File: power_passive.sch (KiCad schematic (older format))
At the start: 39 parts, among them J10 Conn_01x02, J11 Conn_01x02, J12 Conn_01x02, J13 Conn_01x02, J14 Conn_01x02, J15 Conn_01x02, J16 Conn_01x02, J17 Conn_01x02, J18 Conn_01x02, J19 Conn_01x02, J20 Conn_01x02, J5 ATX-24, J6 Conn_01x02, J7 Conn_01x02, J8 Conn_01x02, J9 Conn_01x02, Q1 MMBT4401-7-F, Q10 MMBT4401-7-F, Q11 SI7113ADN-T1-GE3, Q2 MMBT4401-7-F, Q3 MMBT4401-7-F, Q4 SI7113ADN-T1-GE3, Q5 SI7113ADN-T1-GE3, Q6 MMBT4401-7-F, Q7 MMBT4401-7-F, Q8 SI7113ADN-T1-GE3, Q9 SI7113ADN-T1-GE3

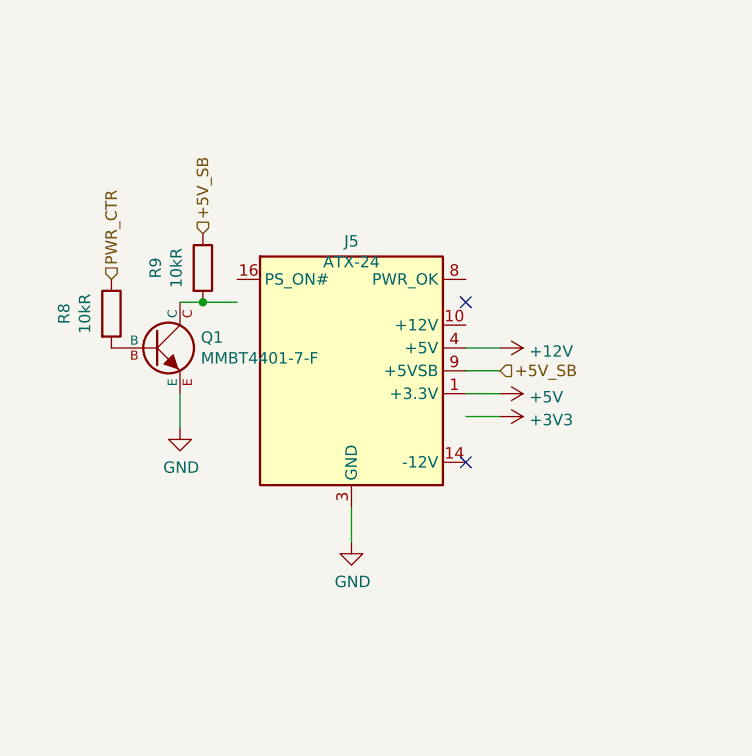
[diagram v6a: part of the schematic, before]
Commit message: Changed ATX-24 symbol to merged version.
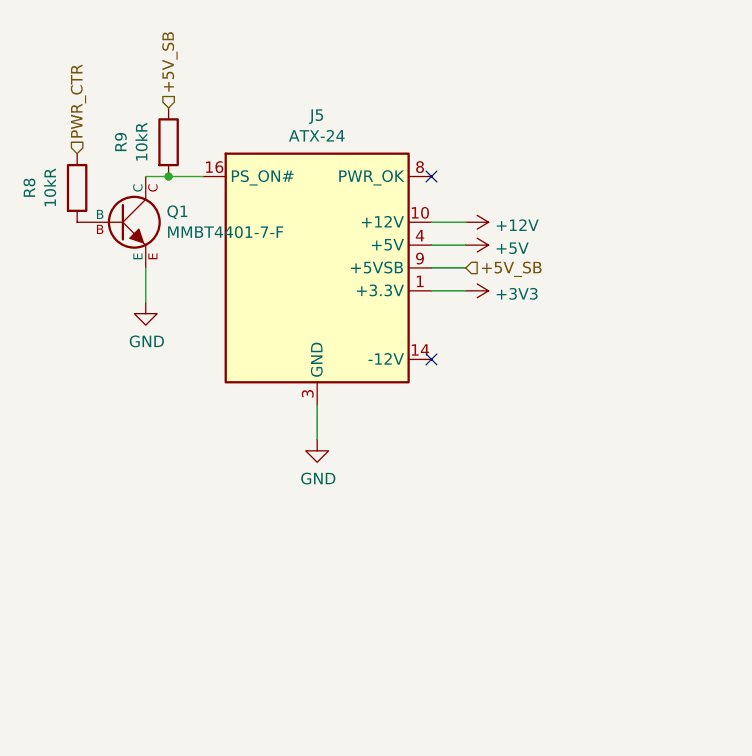
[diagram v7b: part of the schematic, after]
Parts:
- J5: manf# 39-29-9246 -> (none)
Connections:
- net +12V: now also J5.10 (+12V), J5.11 (+12V); no longer J5.21 (+5V), J5.22 (+5V), J5.23 (+5V), J5.4 (+5V), J5.6 (+5V)
- net +3V3: now also J5.1 (+3.3V), J5.12 (+3.3V), J5.13 (+3.3V), J5.2 (+3.3V)
- net +5V: now also J5.21 (+5V), J5.22 (+5V), J5.23 (+5V), J5.4 (+5V), J5.6 (+5V); no longer J5.1 (+3.3V), J5.12 (+3.3V), J5.13 (+3.3V), J5.2 (+3.3V)
- net at J5.16 (PS_ON#): now also Q1.C, R9.2
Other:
- moved on the sheet: Q1, R8, R9
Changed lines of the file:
@@
 $EndComp
 Wire Wire Line
-	3900 2200 4050 2200
-Wire Wire Line
-	3900 2300 4050 2300
-Wire Wire Line
-	3900 2400 4050 2400
-Wire Wire Line
-	3900 2500 4050 2500
-Wire Wire Line
-	3400 2900 3400 3050
-NoConn ~ 3900 2000
-NoConn ~ 3900 2700
+	3750 1650 3900 1650
+Wire Wire Line
+	3750 1850 3900 1850
+Wire Wire Line
+	3750 1750 3900 1750
+Wire Wire Line
+	3750 1950 3900 1950
+Wire Wire Line
+	3250 2450 3250 2600
 $Comp
 L power:GND #PWR?
 U 1 1 5E43306F
-P 3400 3050
+P 3250 2600
 AR Path="/5E43306F" Ref="#PWR?"  Part="1"
 AR Path="/5E4060AB/5E43306F" Ref="#PWR018"  Part="1"
-F 0 "#PWR018" H 3400 2800 50  0001 C CNN
-F 1 "GND" H 3405 2877 50  0000 C CNN
-F 2 "" H 3400 3050 50  0001 C CNN
-F 3 "" H 3400 3050 50  0001 C CNN
-	1    3400 3050
+F 0 "#PWR018" H 3250 2350 50  0001 C CNN
+F 1 "GND" H 3255 2427 50  0000 C CNN
+F 2 "" H 3250 2600 50  0001 C CNN
+F 3 "" H 3250 2600 50  0001 C CNN
+	1    3250 2600
 	1    0    0    -1
 $EndComp
@@
 L power:+12V #PWR?
 U 1 1 5E433076
-P 4050 2200
+P 3900 1650
 AR Path="/5E433076" Ref="#PWR?"  Part="1"
 AR Path="/5E4060AB/5E433076" Ref="#PWR019"  Part="1"
-F 0 "#PWR019" H 4050 2050 50  0001 C CNN
-F 1 "+12V" V 4065 2328 50  0000 L CNN
-F 2 "" H 4050 2200 50  0001 C CNN
-F 3 "" H 4050 2200 50  0001 C CNN
-	1    4050 2200
+F 0 "#PWR019" H 3900 1500 50  0001 C CNN
+F 1 "+12V" V 3915 1778 50  0000 L CNN
+F 2 "" H 3900 1650 50  0001 C CNN
+F 3 "" H 3900 1650 50  0001 C CNN
+	1    3900 1650
 	0    1    1    0
 $EndComp
@@
 L power:+5V #PWR?
 U 1 1 5E43307C
-P 4050 2400
+P 3900 1750
 AR Path="/5E43307C" Ref="#PWR?"  Part="1"
 AR Path="/5E4060AB/5E43307C" Ref="#PWR020"  Part="1"
-F 0 "#PWR020" H 4050 2250 50  0001 C CNN
-F 1 "+5V" V 4065 2528 50  0000 L CNN
-F 2 "" H 4050 2400 50  0001 C CNN
-F 3 "" H 4050 2400 50  0001 C CNN
-	1    4050 2400
+F 0 "#PWR020" H 3900 1600 50  0001 C CNN
+F 1 "+5V" V 3915 1878 50  0000 L CNN
+F 2 "" H 3900 1750 50  0001 C CNN
+F 3 "" H 3900 1750 50  0001 C CNN
+	1    3900 1750
 	0    1    1    0
 $EndComp
@@
 L power:+3V3 #PWR?
 U 1 1 5E433082
-P 4050 2500
+P 3900 1950
 AR Path="/5E433082" Ref="#PWR?"  Part="1"
 AR Path="/5E4060AB/5E433082" Ref="#PWR021"  Part="1"
-F 0 "#PWR021" H 4050 2350 50  0001 C CNN
-F 1 "+3V3" V 4065 2628 50  0000 L CNN
-F 2 "" H 4050 2500 50  0001 C CNN
-F 3 "" H 4050 2500 50  0001 C CNN
-	1    4050 2500
+F 0 "#PWR021" H 3900 1800 50  0001 C CNN
+F 1 "+3V3" V 3915 2078 50  0000 L CNN
+F 2 "" H 3900 1950 50  0001 C CNN
+F 3 "" H 3900 1950 50  0001 C CNN
+	1    3900 1950
 	0    1    1    0
 $EndComp
-Text HLabel 4050 2300 2    50   Input ~ 0
+Text HLabel 3900 1850 2    50   Input ~ 0
 +5V_SB
-$Comp
-L Connector:ATX-24 J5
-U 1 1 5E29B35F
-P 3400 2300
-F 0 "J5" H 3400 2867 50  0000 C CNN
-F 1 "ATX-24" H 3400 2776 50  0000 C CNN
-F 2 "Connector_Molex:Molex_Mini-Fit_Jr_5566-24A_2x12_P4.20mm_Vertical" H 3400 2200 50  0001 C CNN
-F 3 "https://www.intel.com/content/dam/www/public/us/en/documents/guides/power-supply-design-guide-june.pdf#page=33" H 5800 1750 50  0001 C CNN
-F 4 "39-29-9246" H 3400 2300 50  0001 C CNN "manf#"
-	1    3400 2300
-	1    0    0    -1
-$EndComp
 $Comp
 L Connector_Generic:Conn_01x02 J?
@@
 	8600 5450 8600 5950
 Wire Wire Line
-	2650 2000 2750 2000
-Text HLabel 2350 1900 1    50   Input ~ 0
+	2500 1450 2600 1450
+Text HLabel 2200 1350 1    50   Input ~ 0
 PWR_CTR
 $Comp
 L power:GND #PWR?
 U 1 1 5E392A21
-P 2650 2550
+P 2500 2000
 AR Path="/5E392A21" Ref="#PWR?"  Part="1"
 AR Path="/5E4060AB/5E392A21" Ref="#PWR017"  Part="1"
-F 0 "#PWR017" H 2650 2300 50  0001 C CNN
-F 1 "GND" H 2655 2377 50  0000 C CNN
-F 2 "" H 2650 2550 50  0001 C CNN
-F 3 "" H 2650 2550 50  0001 C CNN
-	1    2650 2550
-	1    0    0    -1
-$EndComp
-Wire Wire Line
-	2650 2400 2650 2550
+F 0 "#PWR017" H 2500 1750 50  0001 C CNN
+F 1 "GND" H 2505 1827 50  0000 C CNN
+F 2 "" H 2500 2000 50  0001 C CNN
+F 3 "" H 2500 2000 50  0001 C CNN
+	1    2500 2000
+	1    0    0    -1
+$EndComp
+Wire Wire Line
+	2500 1850 2500 2000
 $Comp
 L lsts-discrete:NPN_EBC Q?
 U 1 1 5E37C7C2
-P 2550 2200
+P 2400 1650
 AR Path="/5E37C7C2" Ref="Q?"  Part="1"
 AR Path="/5E1C04CF/5E37C7C2" Ref="Q?"  Part="1"
@@
 AR Path="/5E4850C0/5E37C7C2" Ref="Q?"  Part="1"
 AR Path="/5E4060AB/5E37C7C2" Ref="Q1"  Part="1"
-F 0 "Q1" H 2741 2246 50  0000 L CNN
-F 1 "MMBT4401-7-F" H 2741 2155 50  0000 L CNN
-F 2 "lsts-discretes:SOT23_BC817" H 2750 2300 50  0001 C CNN
-F 3 "~" H 2550 2200 50  0001 C CNN
-F 4 "MMBT4401-7-F" H 2550 2200 50  0001 C CNN "manf#"
-	1    2550 2200
+F 0 "Q1" H 2591 1696 50  0000 L CNN
+F 1 "MMBT4401-7-F" H 2591 1605 50  0000 L CNN
+F 2 "lsts-discretes:SOT23_BC817" H 2600 1750 50  0001 C CNN
+F 3 "~" H 2400 1650 50  0001 C CNN
+F 4 "MMBT4401-7-F" H 2400 1650 50  0001 C CNN "manf#"
+	1    2400 1650
 	1    0    0    -1
 $EndComp
@@
 L Device:R R?
 U 1 1 5E37C7BB
-P 2350 2050
+P 2200 1500
 AR Path="/5E37C7BB" Ref="R?"  Part="1"
 AR Path="/5E1C04CF/5E37C7BB" Ref="R?"  Part="1"
@@
 AR Path="/5E4850C0/5E37C7BB" Ref="R?"  Part="1"
 AR Path="/5E4060AB/5E37C7BB" Ref="R8"  Part="1"
-F 0 "R8" V 2143 2050 50  0000 C CNN
-F 1 "10kR" V 2234 2050 50  0000 C CNN
-F 2 "lsts-passives:R_0603" V 2280 2050 50  0001 C CNN
-F 3 "~" H 2350 2050 50  0001 C CNN
-F 4 "CRCW060310K0JNEBC" H 2350 2050 50  0001 C CNN "manf#"
-	1    2350 2050
+F 0 "R8" V 1993 1500 50  0000 C CNN
+F 1 "10kR" V 2084 1500 50  0000 C CNN
+F 2 "lsts-passives:R_0603" V 2130 1500 50  0001 C CNN
+F 3 "~" H 2200 1500 50  0001 C CNN
+F 4 "CRCW060310K0JNEBC" H 2200 1500 50  0001 C CNN "manf#"
+	1    2200 1500
 	1    0    0    -1
 $EndComp
@@
 L Device:R R?
 U 1 1 5E39FAB3
-P 2750 1850
+P 2600 1300
 AR Path="/5E39FAB3" Ref="R?"  Part="1"
 AR Path="/5E1C04CF/5E39FAB3" Ref="R?"  Part="1"
@@
 AR Path="/5E4850C0/5E39FAB3" Ref="R?"  Part="1"
 AR Path="/5E4060AB/5E39FAB3" Ref="R9"  Part="1"
-F 0 "R9" V 2543 1850 50  0000 C CNN
-F 1 "10kR" V 2634 1850 50  0000 C CNN
-F 2 "lsts-passives:R_0603" V 2680 1850 50  0001 C CNN
-F 3 "~" H 2750 1850 50  0001 C CNN
-F 4 "CRCW060310K0JNEBC" H 2750 1850 50  0001 C CNN "manf#"
-	1    2750 1850
-	1    0    0    -1
-$EndComp
-Connection ~ 2750 2000
-Wire Wire Line
-	2750 2000 2900 2000
-Text HLabel 2750 1700 1    50   Input ~ 0
+F 0 "R9" V 2393 1300 50  0000 C CNN
+F 1 "10kR" V 2484 1300 50  0000 C CNN
+F 2 "lsts-passives:R_0603" V 2530 1300 50  0001 C CNN
+F 3 "~" H 2600 1300 50  0001 C CNN
+F 4 "CRCW060310K0JNEBC" H 2600 1300 50  0001 C CNN "manf#"
+	1    2600 1300
+	1    0    0    -1
+$EndComp
+Connection ~ 2600 1450
+Wire Wire Line
+	2600 1450 2750 1450
+Text HLabel 2600 1150 1    50   Input ~ 0
 +5V_SB
 Wire Wire Line
@@
 	1    0    0    -1
 $EndComp
+$Comp
+L Connector:ATX-24 J5
+U 1 1 5E8B6E5E
+P 3250 1850
+F 0 "J5" H 3250 2517 50  0000 C CNN
+F 1 "ATX-24" H 3250 2426 50  0000 C CNN
+F 2 "Connector_Molex:Molex_Mini-Fit_Jr_5566-24A_2x12_P4.20mm_Vertical" H 3250 1750 50  0001 C CNN
+F 3 "https://www.intel.com/content/dam/www/public/us/en/documents/guides/power-supply-design-guide-june.pdf#page=33" H 5650 1300 50  0001 C CNN
+	1    3250 1850
+	1    0    0    -1
+$EndComp
+NoConn ~ 3750 1450
+NoConn ~ 3750 2250
 $EndSCHEMATC

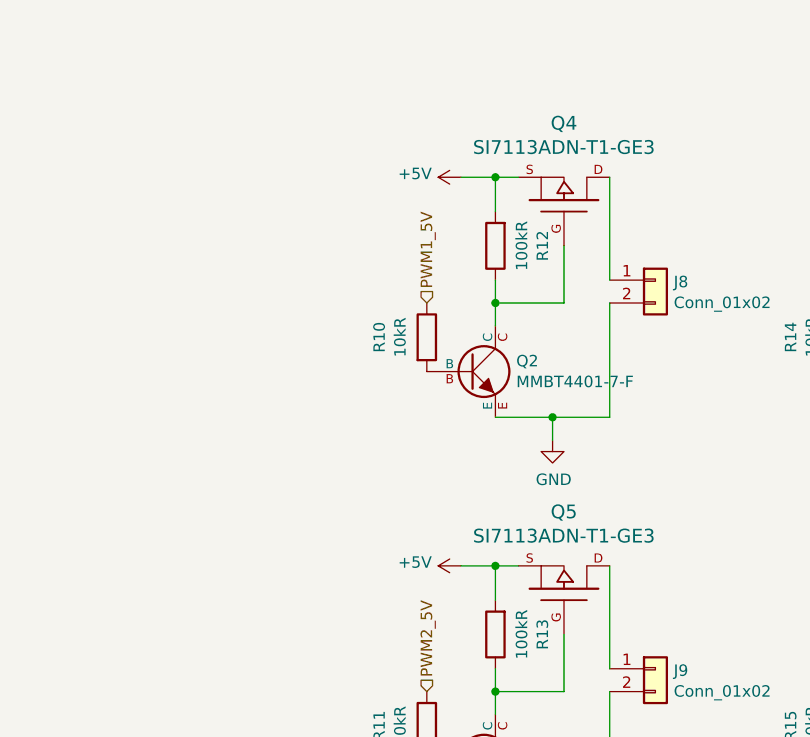
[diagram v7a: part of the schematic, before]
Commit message: Switch PMW 1 & 2 to 12V
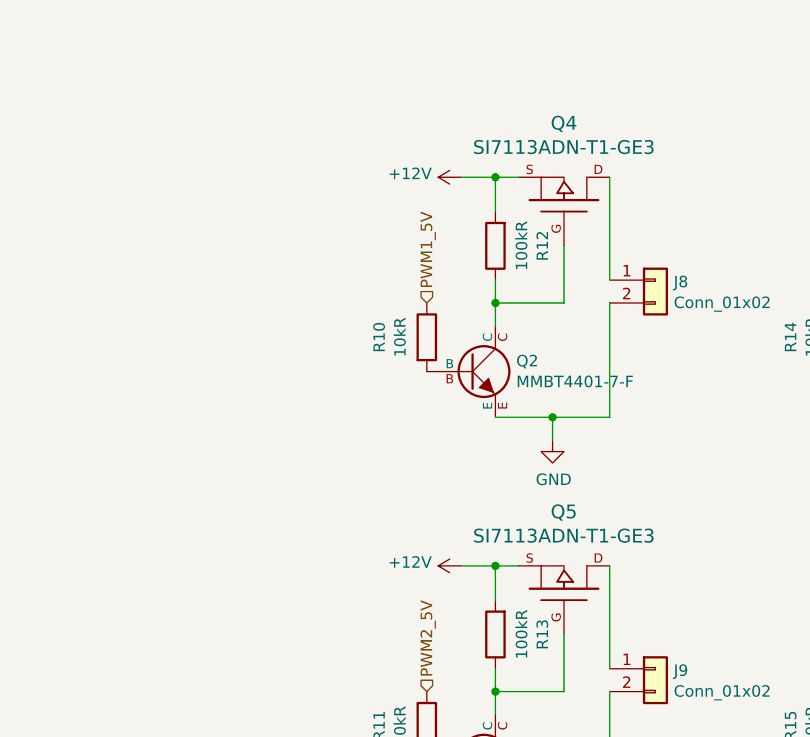
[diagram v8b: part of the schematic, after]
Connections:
- net +12V: now also Q4.S, Q5.S, R12.2, R13.2
- net +5V: no longer Q4.S, Q5.S, R12.2, R13.2
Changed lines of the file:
@@
 Text HLabel 6000 3750 1    50   Input ~ 0
 PWM1_5V
-$Comp
-L power:+5V #PWR026
-U 1 1 5E6D741E
-P 6150 3200
-F 0 "#PWR026" H 6150 3050 50  0001 C CNN
-F 1 "+5V" V 6165 3328 50  0000 L CNN
-F 2 "" H 6150 3200 50  0001 C CNN
-F 3 "" H 6150 3200 50  0001 C CNN
-	1    6150 3200
-	0    -1   -1   0
-$EndComp
 Wire Wire Line
 	6800 3200 6800 3650
@@
 Text HLabel 7800 5450 1    50   Input ~ 0
 PWM4_5V
-$Comp
-L power:+5V #PWR027
-U 1 1 5E7404EE
-P 6150 4900
-F 0 "#PWR027" H 6150 4750 50  0001 C CNN
-F 1 "+5V" V 6165 5028 50  0000 L CNN
-F 2 "" H 6150 4900 50  0001 C CNN
-F 3 "" H 6150 4900 50  0001 C CNN
-	1    6150 4900
-	0    -1   -1   0
-$EndComp
 Wire Wire Line
 	6800 4900 6800 5350
@@
 Text HLabel 9600 3750 1    50   Input ~ 0
 PWM5_5V
-$Comp
-L power:+5V #PWR035
-U 1 1 5E7533B9
-P 7950 4900
-F 0 "#PWR035" H 7950 4750 50  0001 C CNN
-F 1 "+5V" V 7965 5028 50  0000 L CNN
-F 2 "" H 7950 4900 50  0001 C CNN
-F 3 "" H 7950 4900 50  0001 C CNN
-	1    7950 4900
-	0    -1   -1   0
-$EndComp
 Wire Wire Line
 	8600 4900 8600 5350
@@
 NoConn ~ 3750 1450
 NoConn ~ 3750 2250
+$Comp
+L power:+5V #PWR035
+U 1 1 5E7533B9
+P 7950 4900
+F 0 "#PWR035" H 7950 4750 50  0001 C CNN
+F 1 "+5V" V 7965 5028 50  0000 L CNN
+F 2 "" H 7950 4900 50  0001 C CNN
+F 3 "" H 7950 4900 50  0001 C CNN
+	1    7950 4900
+	0    -1   -1   0
+$EndComp
+$Comp
+L power:+12V #PWR?
+U 1 1 5ECFD70E
+P 6150 3200
+F 0 "#PWR?" H 6150 3050 50  0001 C CNN
+F 1 "+12V" V 6165 3328 50  0000 L CNN
+F 2 "" H 6150 3200 50  0001 C CNN
+F 3 "" H 6150 3200 50  0001 C CNN
+	1    6150 3200
+	0    -1   -1   0
+$EndComp
+$Comp
+L power:+12V #PWR?
+U 1 1 5ECFDE1E
+P 6150 4900
+F 0 "#PWR?" H 6150 4750 50  0001 C CNN
+F 1 "+12V" V 6165 5028 50  0000 L CNN
+F 2 "" H 6150 4900 50  0001 C CNN
+F 3 "" H 6150 4900 50  0001 C CNN
+	1    6150 4900
+	0    -1   -1   0
+$EndComp
 $EndSCHEMATC
